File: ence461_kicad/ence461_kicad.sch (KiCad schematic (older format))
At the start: 56 parts, among them U1 LMV324, U2 LMV324, U3 LMV324, U4 74HC3G14DP, U5 LMV321, U6 NCV7344D13R2GOSCT-ND, U7 TPS717DRV-WSON, U8 TPS71433DRVR

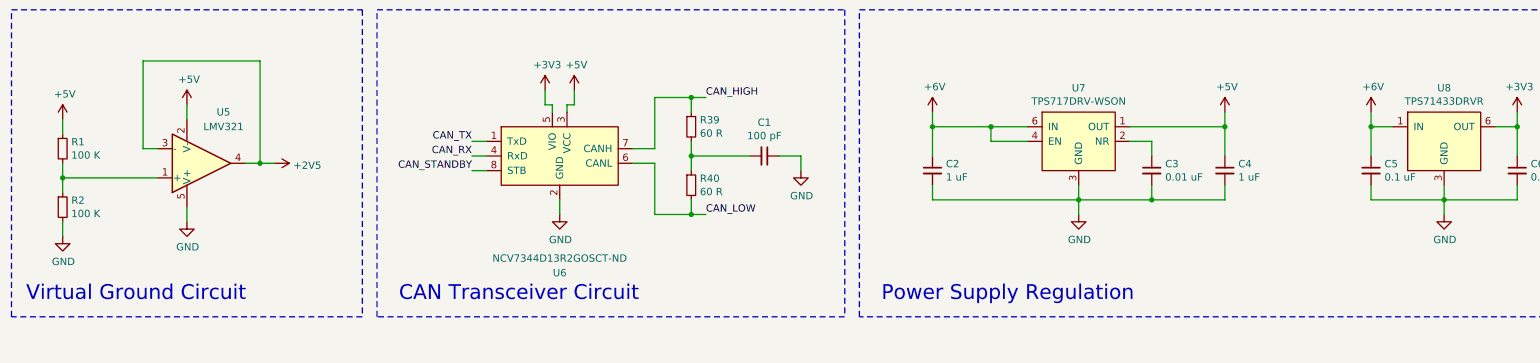
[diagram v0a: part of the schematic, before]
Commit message: 3V3 thermal calc, explain design preference
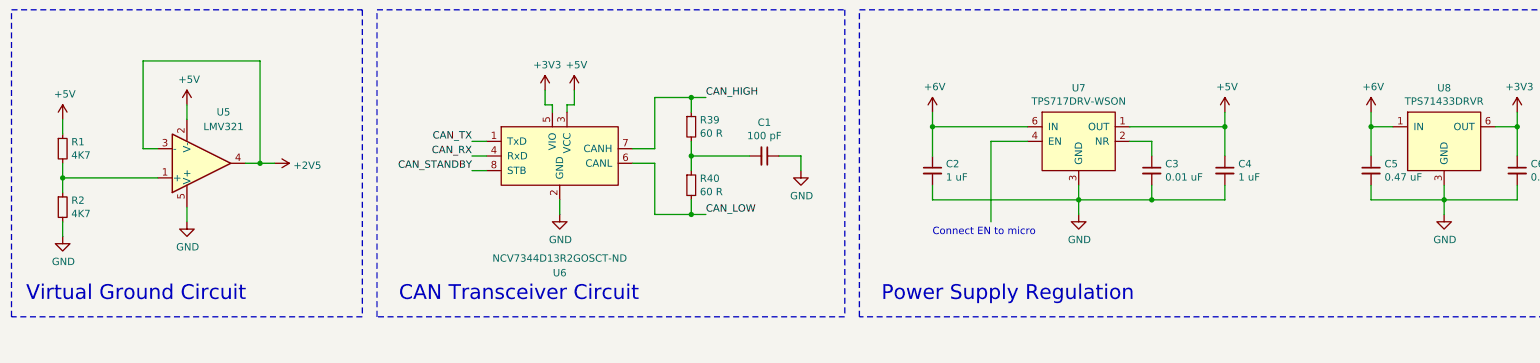
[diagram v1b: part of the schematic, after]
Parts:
- C5: value 0.1 uF -> 0.47 uF
- R1, R2: value 100 K -> 4K7
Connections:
- net +6V: no longer U7.4 (EN)
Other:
- note added: "Connect EN to micro"
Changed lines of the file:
@@
 P 1050 10000
 F 0 "R1" H 1109 10046 50  0000 L CNN
-F 1 "100 K" H 1109 9955 50  0000 L CNN
+F 1 "4K7" H 1109 9955 50  0000 L CNN
 F 2 "" H 1050 10000 50  0001 C CNN
 F 3 "~" H 1050 10000 50  0001 C CNN
@@
 P 1050 10400
 F 0 "R2" H 1109 10446 50  0000 L CNN
-F 1 "100 K" H 1109 10355 50  0000 L CNN
+F 1 "4K7" H 1109 10355 50  0000 L CNN
 F 2 "" H 1050 10400 50  0001 C CNN
 F 3 "~" H 1050 10400 50  0001 C CNN
@@
 	7000 10350 7000 10250
 Wire Wire Line
-	7650 9850 7400 9850
-Wire Wire Line
 	7000 9850 7000 10050
 Wire Wire Line
@@
 Wire Wire Line
 	7650 9950 7400 9950
-Wire Wire Line
-	7400 9950 7400 9850
-Connection ~ 7400 9850
-Wire Wire Line
-	7400 9850 7000 9850
 $Comp
 L power:+6V #PWR029
@@
 P 10000 10150
 F 0 "C5" H 10092 10196 50  0000 L CNN
-F 1 "0.1 uF" H 10092 10105 50  0000 L CNN
+F 1 "0.47 uF" H 10092 10105 50  0000 L CNN
 F 2 "" H 10000 10150 50  0001 C CNN
 F 3 "~" H 10000 10150 50  0001 C CNN
@@
 Text Notes 4000 8450 0    50   ~ 0
 needs programming connector
+Text Notes 7000 10600 0    50   ~ 0
+Connect EN to micro
+Wire Wire Line
+	7000 9850 7650 9850
+Wire Wire Line
+	7400 10500 7400 9950
 $EndSCHEMATC

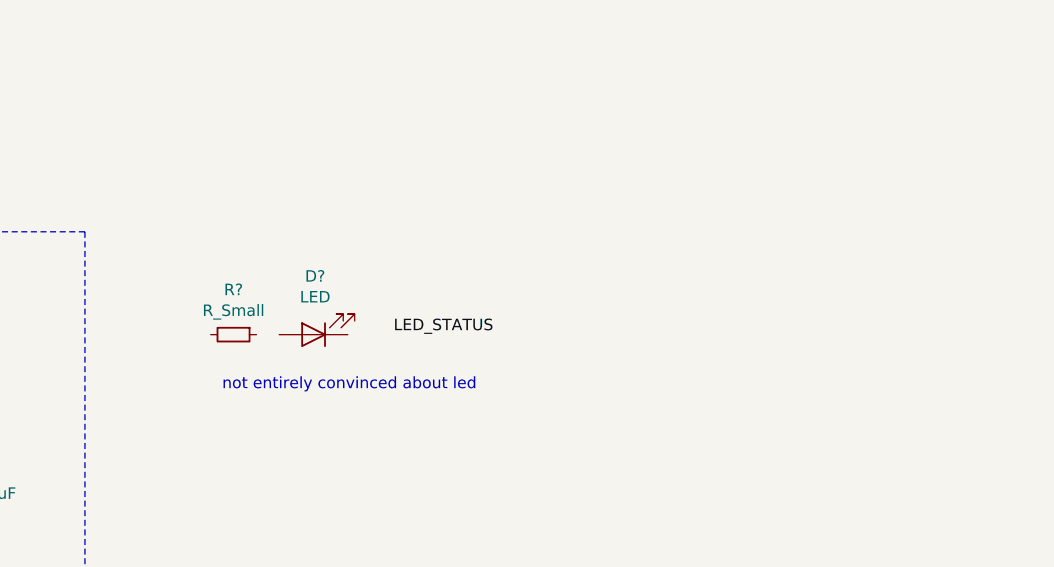
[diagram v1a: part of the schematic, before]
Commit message: Added LED status indicator.
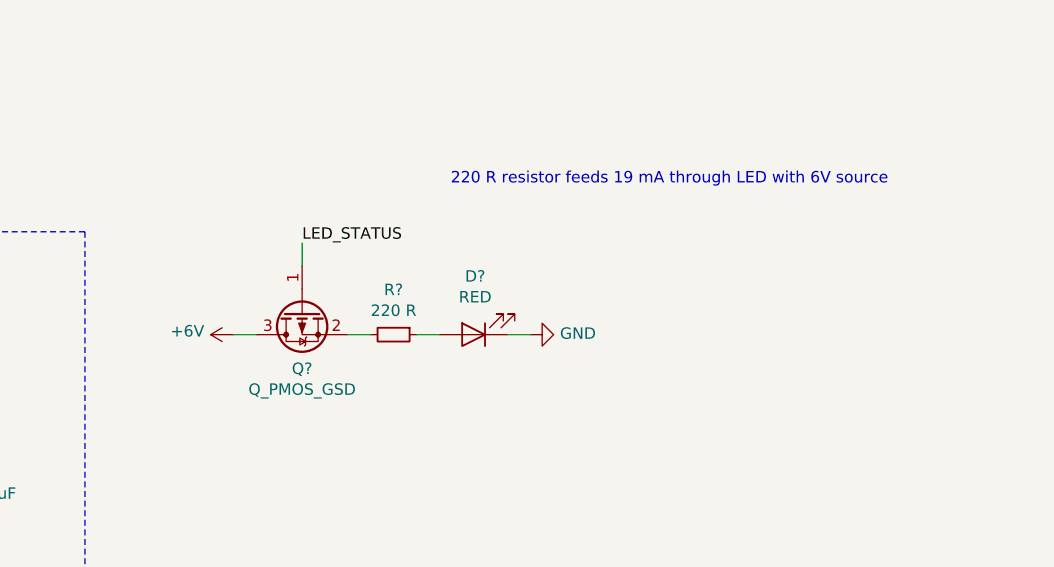
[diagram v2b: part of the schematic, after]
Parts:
- added Q?: Q_PMOS_GSD, symbol Device:Q_PMOS_GSD
- D?: value LED -> RED
- R?: value R_Small -> 220 R
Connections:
- net +6V: now also Q?.3 (D)
- net GND: now also D?.1 (K)
- net LED_STATUS: now also Q?.1 (G)
- net at D?.2 (A): now also R?.1
- net at R?.2: now also Q?.2 (S)
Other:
- note added: "220 R resistor feeds 19 mA through LED with 6V source"
- note removed: "not entirely convinced about led"
- moved on the sheet: D?, R?
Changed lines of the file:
@@
 L Device:LED D?
 U 1 1 5F290098
-P 12650 9500
-F 0 "D?" H 12643 9245 50  0000 C CNN
-F 1 "LED" H 12643 9336 50  0000 C CNN
-F 2 "" H 12650 9500 50  0001 C CNN
-F 3 "~" H 12650 9500 50  0001 C CNN
-	1    12650 9500
+P 13350 9500
+F 0 "D?" H 13343 9245 50  0000 C CNN
+F 1 "RED" H 13343 9336 50  0000 C CNN
+F 2 "" H 13350 9500 50  0001 C CNN
+F 3 "~" H 13350 9500 50  0001 C CNN
+	1    13350 9500
 	-1   0    0    1
 $EndComp
-Text Label 13000 9500 0    50   ~ 0
+Text Label 12600 9100 0    50   ~ 0
 LED_STATUS
 $Comp
 L Device:R_Small R?
 U 1 1 5F2AB002
-P 12300 9500
-F 0 "R?" V 12104 9500 50  0000 C CNN
-F 1 "R_Small" V 12195 9500 50  0000 C CNN
-F 2 "" H 12300 9500 50  0001 C CNN
-F 3 "~" H 12300 9500 50  0001 C CNN
-	1    12300 9500
+P 13000 9500
+F 0 "R?" V 12804 9500 50  0000 C CNN
+F 1 "220 R" V 12895 9500 50  0000 C CNN
+F 2 "" H 13000 9500 50  0001 C CNN
+F 3 "~" H 13000 9500 50  0001 C CNN
+	1    13000 9500
 	0    1    1    0
 $EndComp
-Text Notes 12250 9750 0    50   ~ 0
-not entirely convinced about led
+Text Notes 13250 8850 0    50   ~ 0
+220 R resistor feeds 19 mA through LED with 6V source
 Text Notes 4000 8450 0    50   ~ 0
 needs programming connector
@@
 Wire Wire Line
 	7400 10500 7400 9950
+$Comp
+L Device:Q_PMOS_GSD Q?
+U 1 1 5ECA756A
+P 12600 9400
+F 0 "Q?" V 12849 9400 50  0000 C CNN
+F 1 "Q_PMOS_GSD" V 12940 9400 50  0000 C CNN
+F 2 "" H 12800 9500 50  0001 C CNN
+F 3 "~" H 12600 9400 50  0001 C CNN
+	1    12600 9400
+	0    -1   1    0
+$EndComp
+$Comp
+L power:GND #PWR?
+U 1 1 5ECB9131
+P 13600 9500
+F 0 "#PWR?" H 13600 9250 50  0001 C CNN
+F 1 "GND" V 13605 9372 50  0000 R CNN
+F 2 "" H 13600 9500 50  0001 C CNN
+F 3 "" H 13600 9500 50  0001 C CNN
+	1    13600 9500
+	0    -1   -1   0
+$EndComp
+Wire Wire Line
+	12600 9100 12600 9200
+Wire Wire Line
+	12800 9500 12900 9500
+Wire Wire Line
+	13100 9500 13200 9500
+Wire Wire Line
+	13500 9500 13600 9500
+$Comp
+L power:+6V #PWR?
+U 1 1 5ECF003B
+P 12300 9500
+F 0 "#PWR?" H 12300 9350 50  0001 C CNN
+F 1 "+6V" V 12315 9628 50  0000 L CNN
+F 2 "" H 12300 9500 50  0001 C CNN
+F 3 "" H 12300 9500 50  0001 C CNN
+	1    12300 9500
+	0    -1   -1   0
+$EndComp
+Wire Wire Line
+	12300 9500 12400 9500
 $EndSCHEMATC

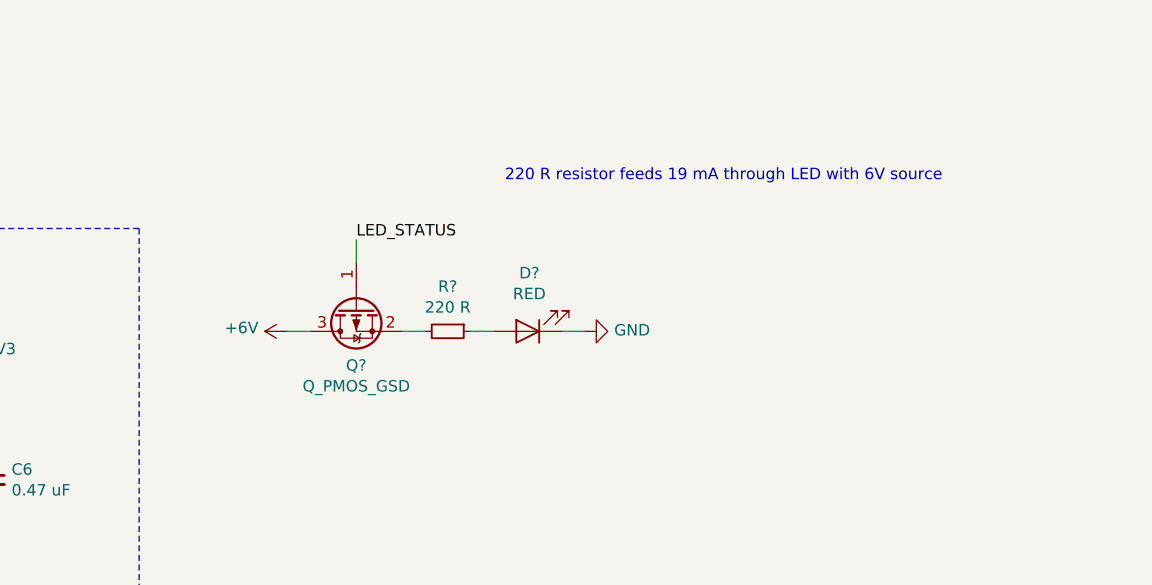
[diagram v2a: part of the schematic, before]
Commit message: Added LED to schematic.
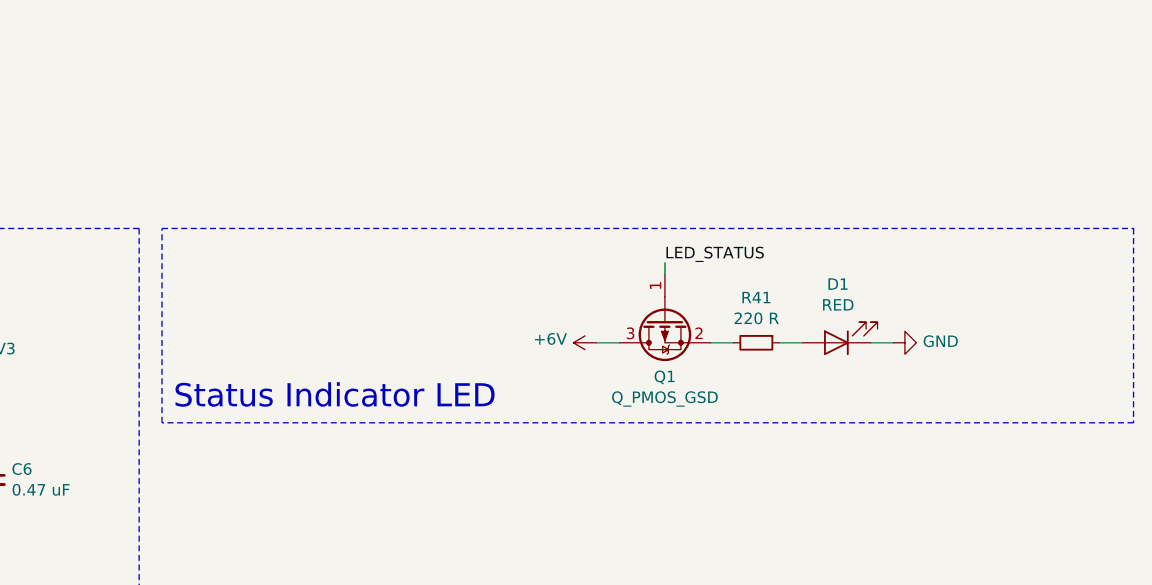
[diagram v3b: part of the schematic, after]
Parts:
- D1: renamed from D?; footprint (none) -> LED_SMD:LED_PLCC-2
- Q1: renamed from Q?; footprint (none) -> Package_TO_SOT_SMD:SOT-723
- gave numbers to parts that had none: 1
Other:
- note added: "Status Indicator LED"
- note removed: "220 R resistor feeds 19 mA through LED with 6V source"
- moved on the sheet: D1, Q1, R41
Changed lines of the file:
@@
 CAN_TX
 $Comp
-L Device:LED D?
+L Device:LED D1
 U 1 1 5F290098
-P 13350 9500
-F 0 "D?" H 13343 9245 50  0000 C CNN
-F 1 "RED" H 13343 9336 50  0000 C CNN
-F 2 "" H 13350 9500 50  0001 C CNN
-F 3 "~" H 13350 9500 50  0001 C CNN
-	1    13350 9500
+P 14700 9550
+F 0 "D1" H 14693 9295 50  0000 C CNN
+F 1 "RED" H 14693 9386 50  0000 C CNN
+F 2 "LED_SMD:LED_PLCC-2" H 14700 9550 50  0001 C CNN
+F 3 "~" H 14700 9550 50  0001 C CNN
+	1    14700 9550
 	-1   0    0    1
 $EndComp
-Text Label 12600 9100 0    50   ~ 0
+Text Label 13950 9200 0    50   ~ 0
 LED_STATUS
 $Comp
-L Device:R_Small R?
+L Device:R_Small R41
 U 1 1 5F2AB002
-P 13000 9500
-F 0 "R?" V 12804 9500 50  0000 C CNN
-F 1 "220 R" V 12895 9500 50  0000 C CNN
-F 2 "" H 13000 9500 50  0001 C CNN
-F 3 "~" H 13000 9500 50  0001 C CNN
-	1    13000 9500
+P 14350 9550
+F 0 "R41" V 14154 9550 50  0000 C CNN
+F 1 "220 R" V 14245 9550 50  0000 C CNN
+F 2 "" H 14350 9550 50  0001 C CNN
+F 3 "~" H 14350 9550 50  0001 C CNN
+	1    14350 9550
 	0    1    1    0
 $EndComp
-Text Notes 13250 8850 0    50   ~ 0
-220 R resistor feeds 19 mA through LED with 6V source
 Text Notes 4000 8450 0    50   ~ 0
 needs programming connector
@@
 	7400 10500 7400 9950
 $Comp
-L Device:Q_PMOS_GSD Q?
+L Device:Q_PMOS_GSD Q1
 U 1 1 5ECA756A
-P 12600 9400
-F 0 "Q?" V 12849 9400 50  0000 C CNN
-F 1 "Q_PMOS_GSD" V 12940 9400 50  0000 C CNN
-F 2 "" H 12800 9500 50  0001 C CNN
-F 3 "~" H 12600 9400 50  0001 C CNN
-	1    12600 9400
+P 13950 9450
+F 0 "Q1" V 14199 9450 50  0000 C CNN
+F 1 "Q_PMOS_GSD" V 14290 9450 50  0000 C CNN
+F 2 "Package_TO_SOT_SMD:SOT-723" H 14150 9550 50  0001 C CNN
+F 3 "~" H 13950 9450 50  0001 C CNN
+	1    13950 9450
 	0    -1   1    0
 $EndComp
 $Comp
-L power:GND #PWR?
+L power:GND #PWR036
 U 1 1 5ECB9131
-P 13600 9500
-F 0 "#PWR?" H 13600 9250 50  0001 C CNN
-F 1 "GND" V 13605 9372 50  0000 R CNN
-F 2 "" H 13600 9500 50  0001 C CNN
-F 3 "" H 13600 9500 50  0001 C CNN
-	1    13600 9500
+P 14950 9550
+F 0 "#PWR036" H 14950 9300 50  0001 C CNN
+F 1 "GND" V 14955 9422 50  0000 R CNN
+F 2 "" H 14950 9550 50  0001 C CNN
+F 3 "" H 14950 9550 50  0001 C CNN
+	1    14950 9550
 	0    -1   -1   0
 $EndComp
 Wire Wire Line
-	12600 9100 12600 9200
+	13950 9200 13950 9250
 Wire Wire Line
-	12800 9500 12900 9500
+	14150 9550 14250 9550
 Wire Wire Line
-	13100 9500 13200 9500
+	14450 9550 14550 9550
 Wire Wire Line
-	13500 9500 13600 9500
+	14850 9550 14950 9550
 $Comp
-L power:+6V #PWR?
+L power:+6V #PWR035
 U 1 1 5ECF003B
-P 12300 9500
-F 0 "#PWR?" H 12300 9350 50  0001 C CNN
-F 1 "+6V" V 12315 9628 50  0000 L CNN
-F 2 "" H 12300 9500 50  0001 C CNN
-F 3 "" H 12300 9500 50  0001 C CNN
-	1    12300 9500
+P 13650 9550
+F 0 "#PWR035" H 13650 9400 50  0001 C CNN
+F 1 "+6V" V 13665 9678 50  0000 L CNN
+F 2 "" H 13650 9550 50  0001 C CNN
+F 3 "" H 13650 9550 50  0001 C CNN
+	1    13650 9550
 	0    -1   -1   0
 $EndComp
 Wire Wire Line
-	12300 9500 12400 9500
+	13650 9550 13750 9550
+Text Notes 11800 9850 0    101  ~ 0
+Status Indicator LED
+Wire Notes Line
+	11750 9900 11750 9050
+Wire Notes Line
+	11750 9050 16000 9050
+Wire Notes Line
+	16000 9050 16000 9900
+Wire Notes Line
+	16000 9900 11750 9900
 $EndSCHEMATC

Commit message: Added micro info.
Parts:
- C1, C2, C3, C4, C5, C6: footprint (none) -> Capacitor_SMD:C_0603_1608Metric
- R1, R10, R11, R12, R13, R14, R15, R16, R17, R18, R19, R2, R20, R21, R22, R23, R24, R25, R26, R27, R28, R29, R3, R30, R31, R32, R33, R34, R35, R36, R37, R38, R39, R4, R40, R41, R5, R6, R7, R8, R9: footprint (none) -> Resistor_SMD:R_0603_1608Metric
- U1, U2, U3: footprint (none) -> Package_SO:TSSOP-14_4.4x5mm_P0.65mm
- U5: footprint (none) -> Package_TO_SOT_SMD:SOT-23-5
